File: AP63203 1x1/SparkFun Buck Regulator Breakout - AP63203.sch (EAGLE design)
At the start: 22 parts, among them U1 AP63203

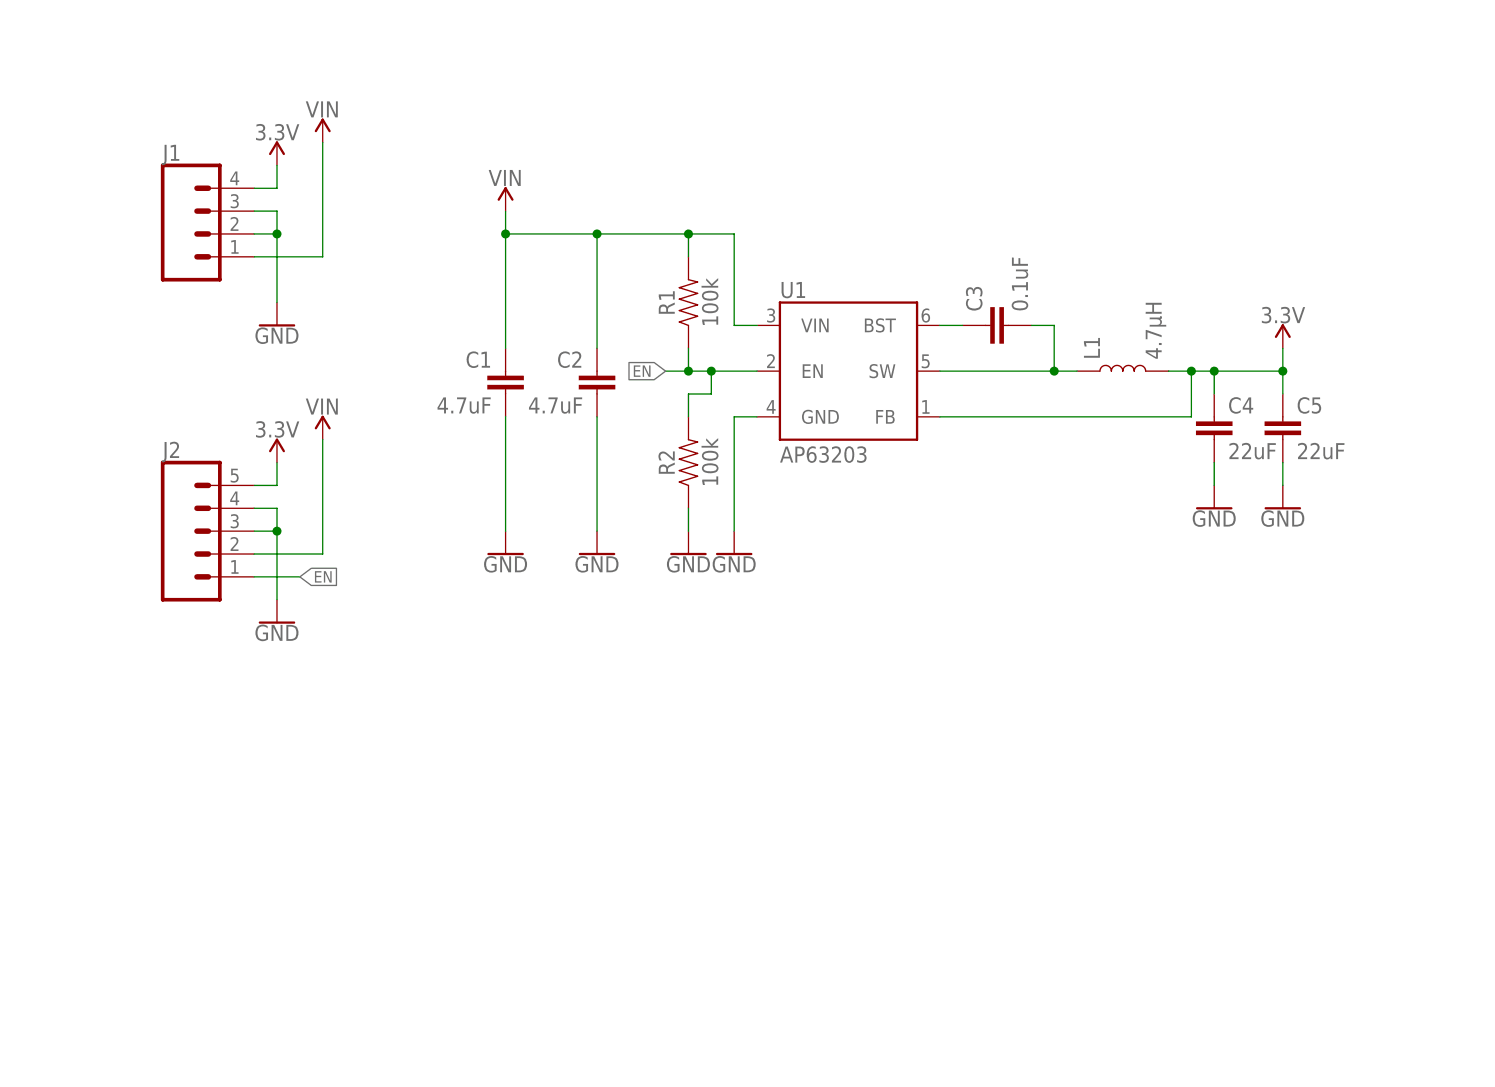
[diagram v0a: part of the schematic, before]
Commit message: v01 update
-Added barrel jack
-Replaced 4.7uF capacitors with 10uF/50V
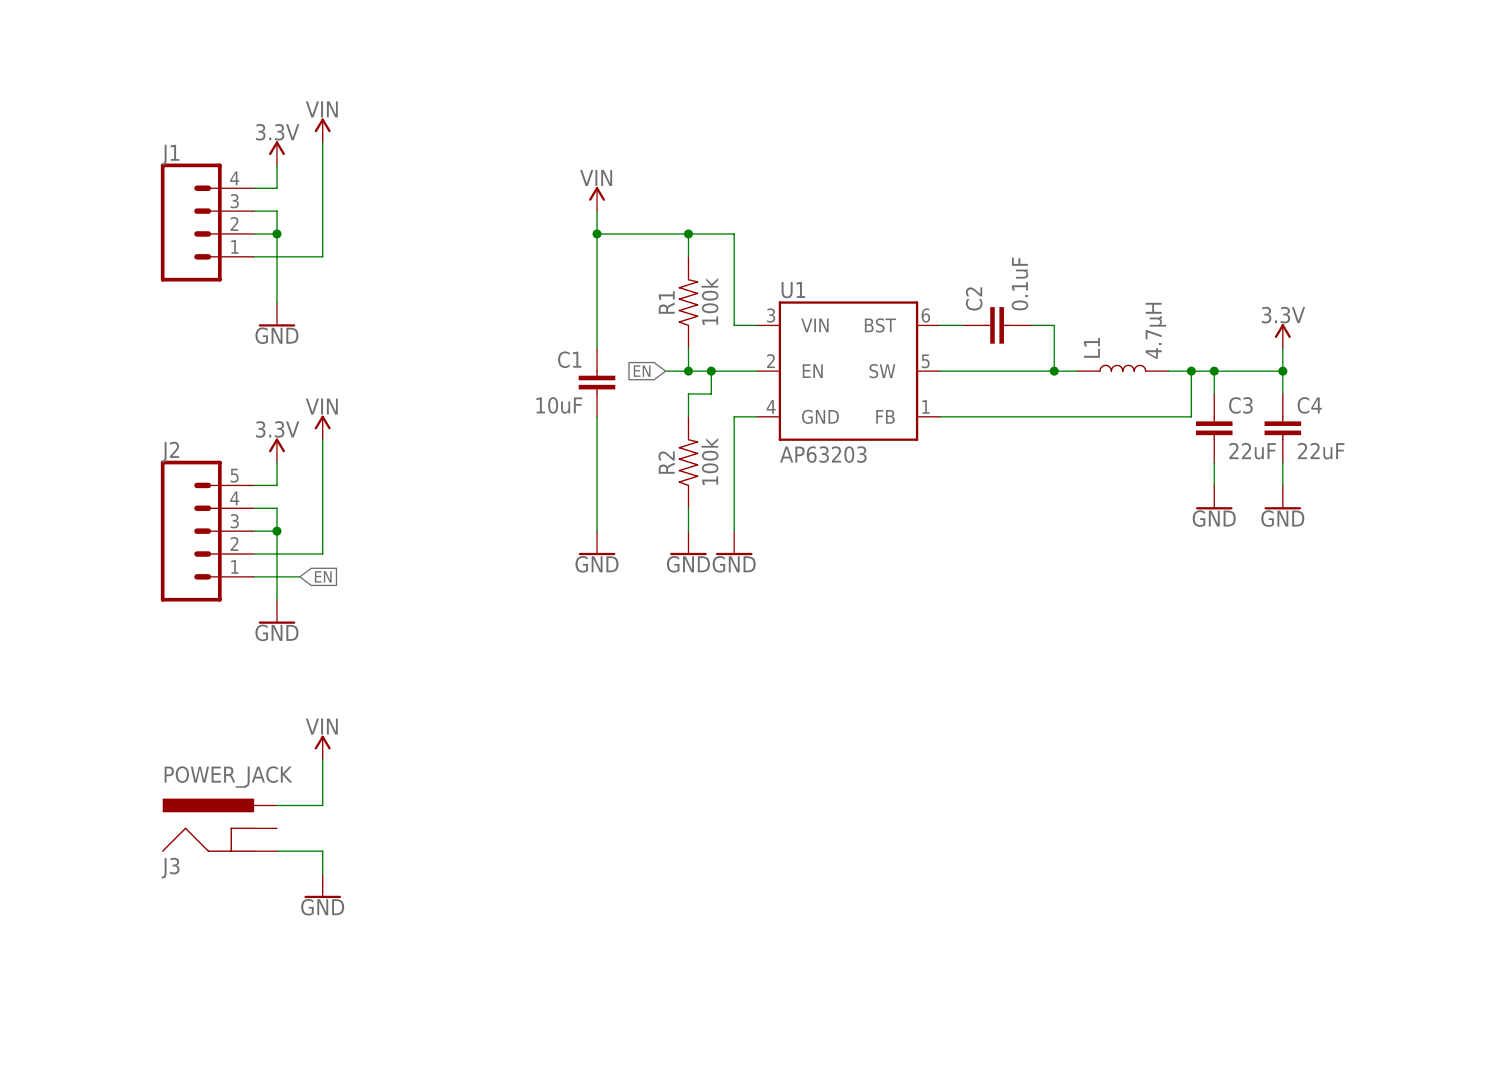
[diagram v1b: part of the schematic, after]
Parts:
- removed C5: 22uF, SparkFun-Capacitors:22UF-0603-6.3V-20%
- added J3: POWER_JACK, SparkFun-Connectors:POWER_JACKPOWER_JACK_SLOT
- C1: value 4.7uF -> 10uF; device SparkFun-Capacitors:4.7UF-0603-35V-(20%) -> SparkFun-Capacitors:10UF-1210-50V-20%
- C2: value 4.7uF -> 0.1uF; device SparkFun-Capacitors:4.7UF-0603-35V-(20%) -> SparkFun-Capacitors:0.1UF-0603-25V-5%
- C3: value 0.1uF -> 22uF; device SparkFun-Capacitors:0.1UF-0603-25V-5% -> SparkFun-Capacitors:22UF-0603-6.3V-20%
- FD2: value FIDUCIAL0.2MM -> FIDUCIALUFIDUCIAL; device SparkFun-Aesthetics:FIDUCIAL0.2MM -> SparkFun-Aesthetics:FIDUCIALUFIDUCIAL
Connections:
- net 3.3V: now also C3.1; no longer C5.1
- net GND: now also C3.2, J3.GND; no longer C2.2, C5.2
- net N$4: now also C2.1; no longer C3.1
- net N$5: now also C2.2; no longer C3.2
- net VIN: now also J3.PWR; no longer C2.1
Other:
- moved on the sheet: C1, C2, C3, C4

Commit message: v01 post view changes
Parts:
- added D1: RED, SparkFun-LED:LED-RED0603
- added LOGO3: SPECIAL_INSTRUCTIONS-ORDERING, SparkFun-Aesthetics:SPECIAL_INSTRUCTIONS-ORDERING
- added PWR: JUMPER-SMT_2_NC_TRACE_SILK, SparkFun-Jumpers:JUMPER-SMT_2_NC_TRACE_SILK
- added R3: 1k, SparkFun-Resistors:1KOHM-0603-1/10W-1%
- LOGO2: value OSHW-LOGOM -> OSHW-LOGOS; device SparkFun-Aesthetics:OSHW-LOGOM -> SparkFun-Aesthetics:OSHW-LOGOS
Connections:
- new net N$1: D1.A, R3.1
- new net N$2: PWR.1, R3.2
- net 3.3V: now also PWR.2
- net GND: now also D1.C
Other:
- note added: "Buck Regulator"
- note added: "Connectors"
- note added: "VIN: 3.8-32V Iout: 2A Max"
- moved on the sheet: C1, C2, C3, C4, L1, R1, R2, U1

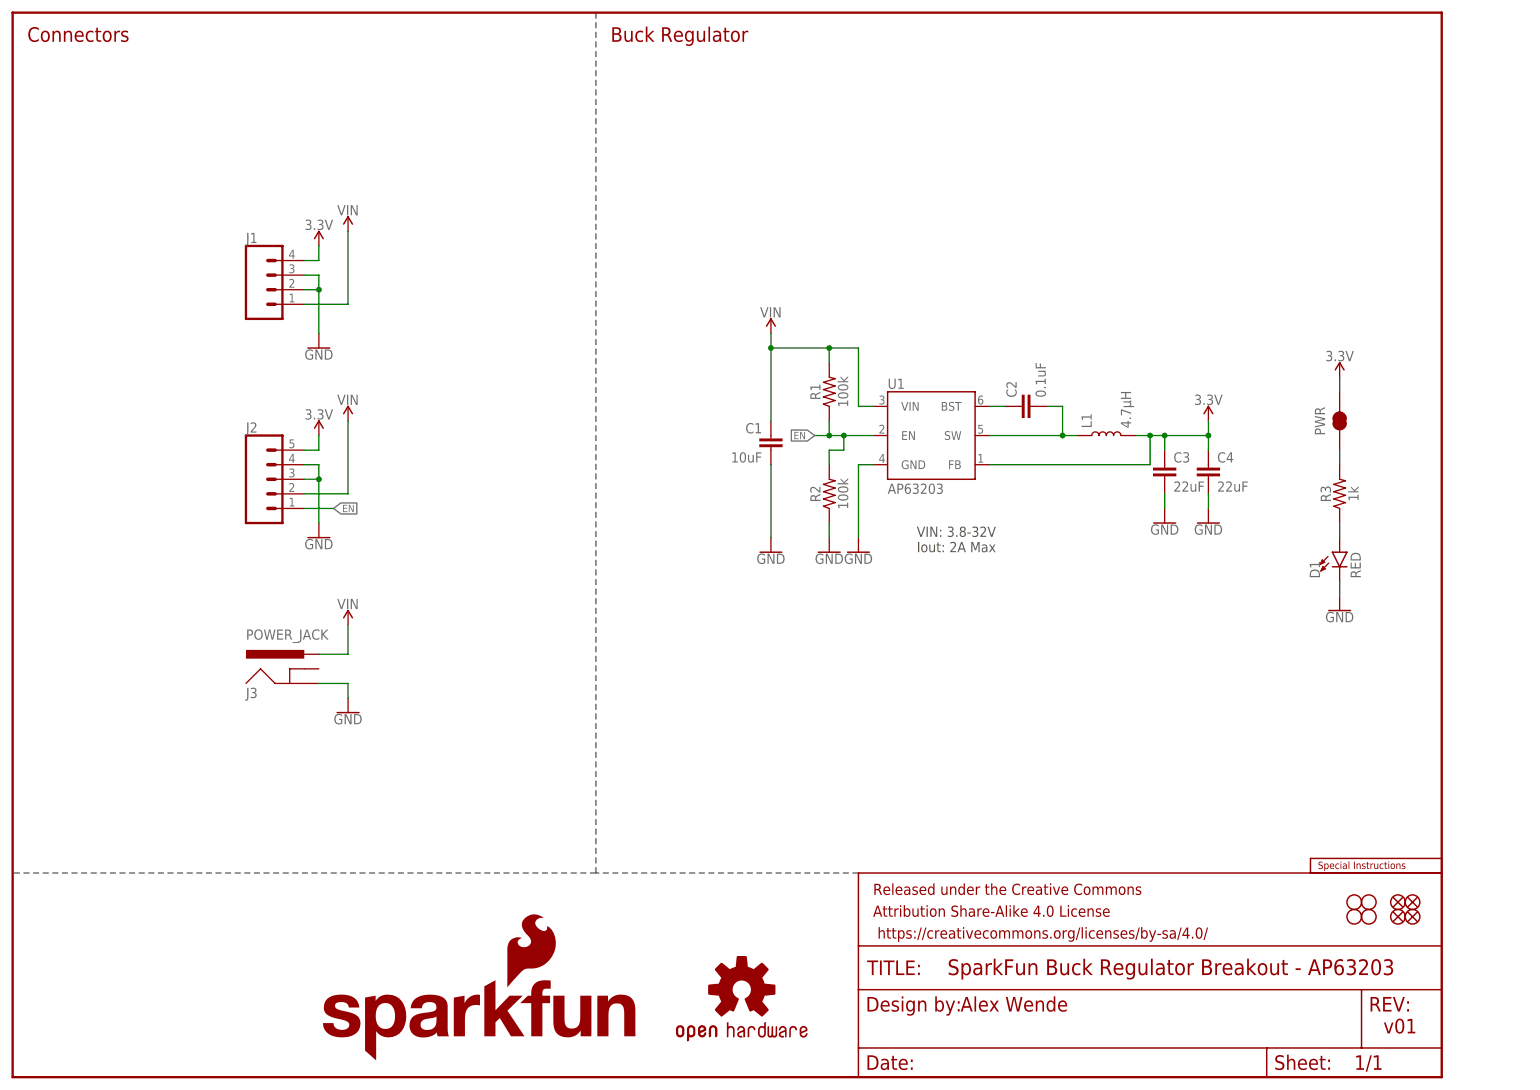
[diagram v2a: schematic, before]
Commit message: Update SparkFun Buck Regulator Breakout - AP63203.sch
Added led jumper note
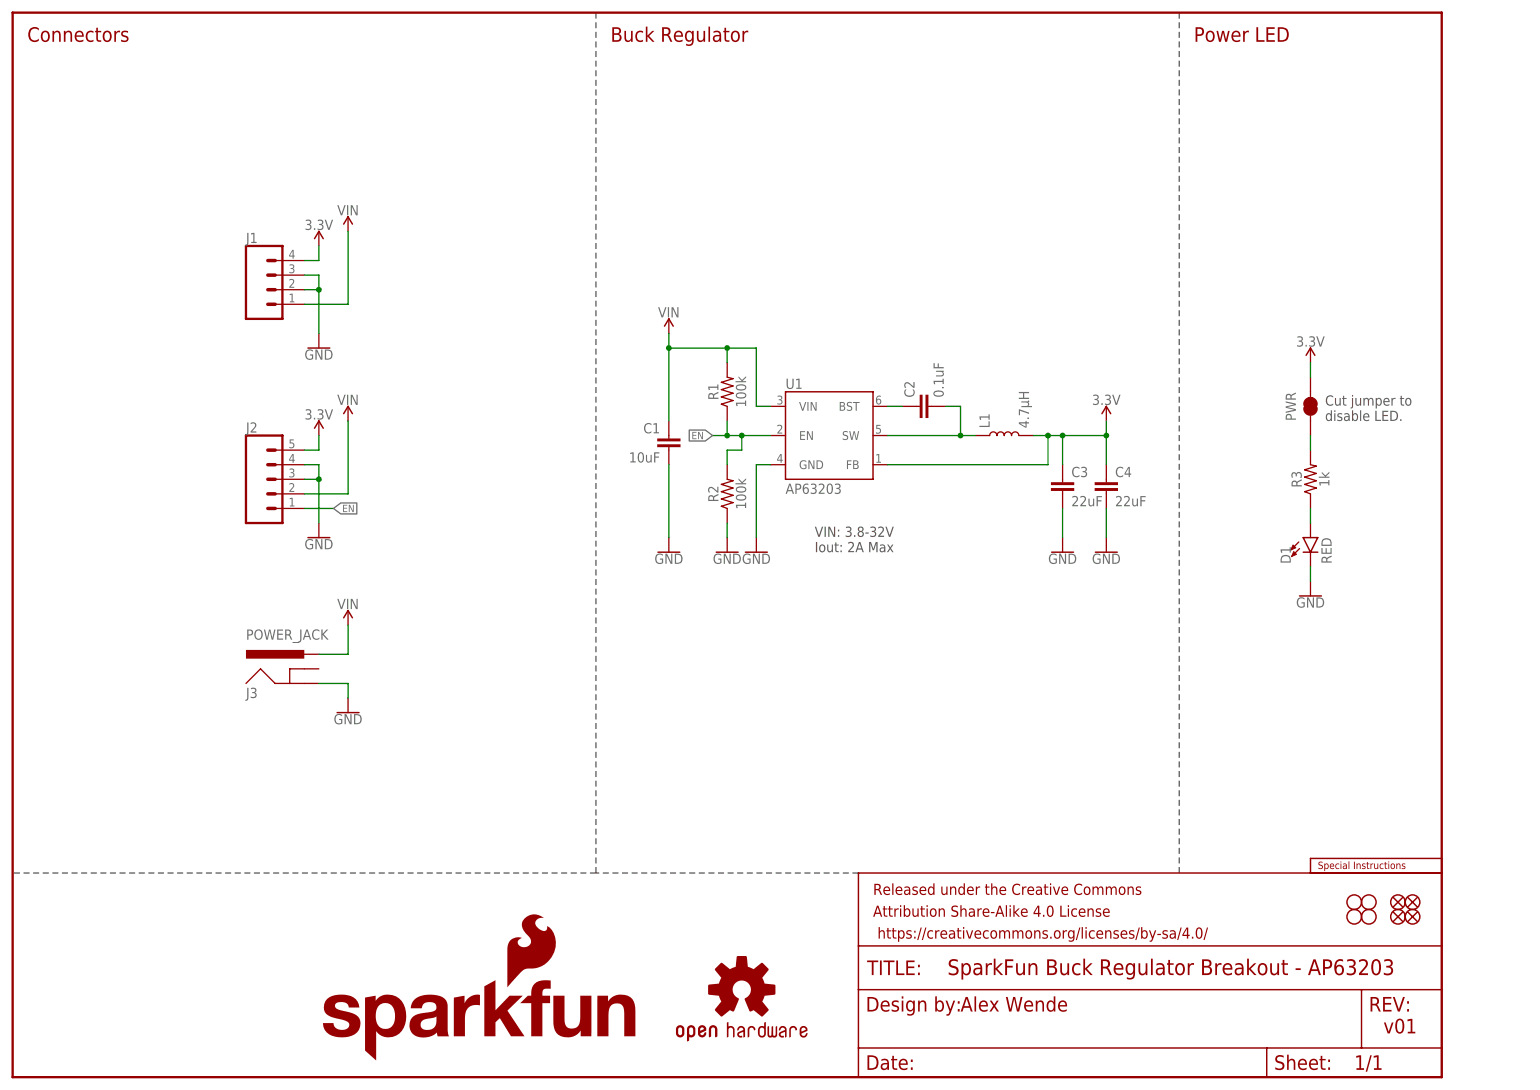
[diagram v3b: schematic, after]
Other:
- note added: "Cut jumper to disable LED."
- note added: "Power LED"
- moved on the sheet: C1, C2, C3, C4, D1, L1, PWR, R1, R2, R3, U1
